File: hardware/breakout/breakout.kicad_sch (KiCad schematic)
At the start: 20 parts, among them J1 24V IN, J2 SPARE, P8 P8, P9 P9, SW1 RESET

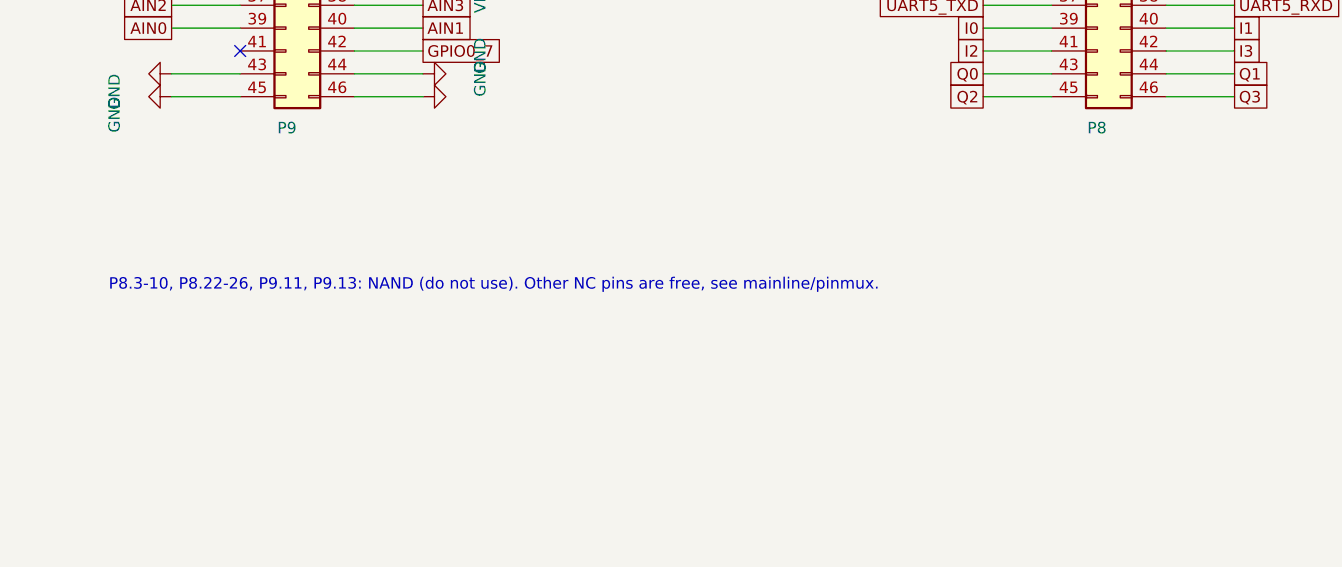
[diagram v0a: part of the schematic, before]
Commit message: Rename mainline/ to firmware/
"mainline" described how the work started (mainline kernel instead of Bitmain 3.8), not
what the directory holds. The repository root now reads hardware/ (KiCad), firmware/ (kernel,
DTS, pinmux, Yocto layer, web UI, tools), docs/, legacy/. Path references and the layer
variable (ANTMINER_FIRMWARE_DIR) updated; "mainline" stays where it means mainline Linux.
Verified: antminer-image and antminer-provision-image build from the new path, the generated
am335x-antminer.dts is unchanged, web smoke test passes, docs links/paths check clean.
Local build trees need the layer path in build/conf/bblayers.conf updated once
(.../repo/firmware/yocto/meta-antminer).

Co-Authored-By: Claude Opus 5.5 <noreply@anthropic.com>
Claude-Session: https://claude.ai/code/session_01WsZ9zSJC7m9WKHj8571c55
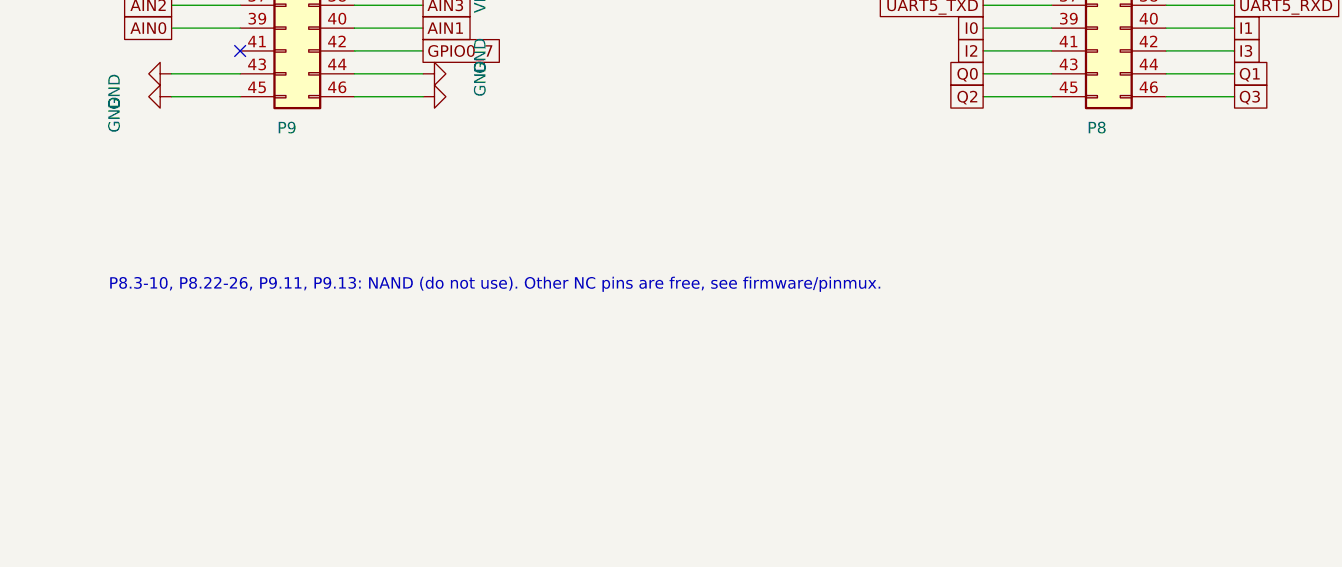
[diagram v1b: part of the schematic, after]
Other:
- note added: "P8.3-10, P8.22-26, P9.11, P9.13: NAND (do not use). Other NC pins are free, see firmware/pinmux."
- note removed: "P8.3-10, P8.22-26, P9.11, P9.13: NAND (do not use). Other NC pins are free, see mainline/pinmux."
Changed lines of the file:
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@@
 		)
 	)
-	(text "P8.3-10, P8.22-26, P9.11, P9.13: NAND (do not use). Other NC pins are free, see mainline/pinmux." (exclude_from_sim no) (at 40 150 0)
+	(text "P8.3-10, P8.22-26, P9.11, P9.13: NAND (do not use). Other NC pins are free, see firmware/pinmux." (exclude_from_sim no) (at 40 150 0)
 		(effects (font (size 1.27 1.27)) (justify left bottom))
 	)
